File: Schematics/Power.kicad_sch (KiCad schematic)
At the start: 12 parts, among them J25 43650-0418, J26 43650-0418, J27 43650-0418, U5 TR05S3V3

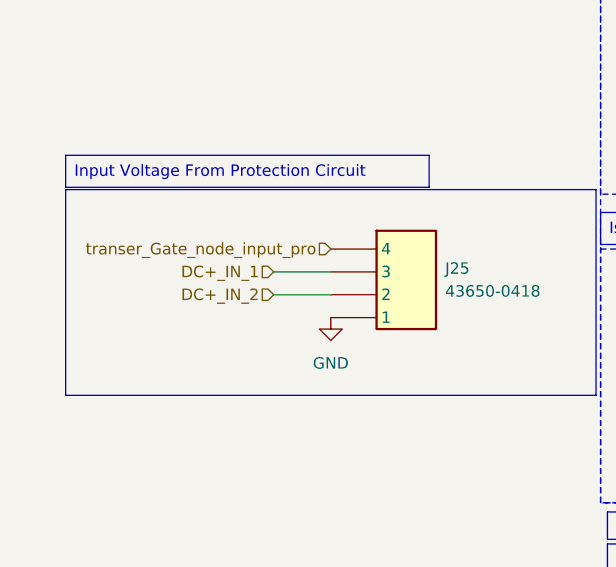
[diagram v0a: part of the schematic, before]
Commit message: WIP PCB Design: Finished DC Input / Protection Circuit
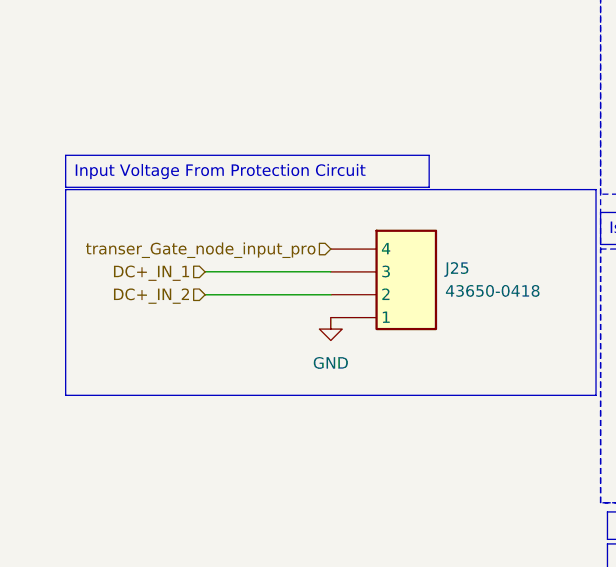
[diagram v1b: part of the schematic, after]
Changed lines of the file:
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@@
 	(wire
 		(pts
-			(xy 46.99 88.9) (xy 53.34 88.9)
+			(xy 39.37 88.9) (xy 53.34 88.9)
 		)
 		(stroke
@@
 	(wire
 		(pts
-			(xy 46.99 86.36) (xy 53.34 86.36)
+			(xy 39.37 86.36) (xy 53.34 86.36)
 		)
 		(stroke
@@
 	(hierarchical_label "DC+_IN_1"
 		(shape input)
-		(at 46.99 86.36 180)
+		(at 39.37 86.36 180)
 		(effects
 			(font
@@
 	(hierarchical_label "DC+_IN_2"
 		(shape input)
-		(at 46.99 88.9 180)
-		(effects
-			(font
-				(size 1.27 1.27)
-			)
-			(justify right)
-		)
-	)
+		(at 39.37 88.9 180)
+		(effects
+			(font
+				(size 1.27 1.27)
+			)
+			(justify right)
+		)
+	)
+	(netclass_flag ""
+		(length 2.54)
+		(shape diamond)
+		(at 97.79 99.06 180)
+		(fields_autoplaced yes)
+		(effects
+			(font
+				(size 1.27 1.27)
+			)
+			(justify right bottom)
+		)
+		(property "Netclass" "5amp"
+			(at 98.9965 101.6 0)
+			(effects
+				(font
+					(size 1.27 1.27)
+				)
+				(justify left)
+			)
+		)
+		(property "Component Class" ""
+			(at -110.49 40.64 0)
+			(effects
+				(font
+					(size 1.27 1.27)
+					(italic yes)
+				)
+			)
+		)
+	)
+	(netclass_flag ""
+		(length 2.54)
+		(shape diamond)
+		(at 41.91 88.9 180)
+		(fields_autoplaced yes)
+		(effects
+			(font
+				(size 1.27 1.27)
+			)
+			(justify right bottom)
+		)
+		(property "Netclass" "5amp"
+			(at 43.1165 91.44 0)
+			(effects
+				(font
+					(size 1.27 1.27)
+				)
+				(justify left)
+			)
+		)
+		(property "Component Class" ""
+			(at -166.37 30.48 0)
+			(effects
+				(font
+					(size 1.27 1.27)
+					(italic yes)
+				)
+			)
+		)
+	)
+	(netclass_flag ""
+		(length 2.54)
+		(shape diamond)
+		(at 45.72 86.36 180)
+		(fields_autoplaced yes)
+		(effects
+			(font
+				(size 1.27 1.27)
+			)
+			(justify right bottom)
+		)
+		(property "Netclass" "5amp"
+			(at 46.9265 88.9 0)
+			(effects
+				(font
+					(size 1.27 1.27)
+				)
+				(justify left)
+			)
+		)
+		(property "Component Class" ""
+			(at -162.56 27.94 0)
+			(effects
+				(font
+					(size 1.27 1.27)
+					(italic yes)
+				)
+			)
+		)
+	)
+	(netclass_flag ""
+		(length 2.54)
+		(shape diamond)
+		(at 97.79 58.42 180)
+		(fields_autoplaced yes)
+		(effects
+			(font
+				(size 1.27 1.27)
+			)
+			(justify right bottom)
+		)
+		(property "Netclass" "5amp"
+			(at 98.9965 60.96 0)
+			(effects
+				(font
+					(size 1.27 1.27)
+				)
+				(justify left)
+			)
+		)
+		(property "Component Class" ""
+			(at -110.49 0 0)
+			(effects
+				(font
+					(size 1.27 1.27)
+					(italic yes)
+				)
+			)
+		)
+	)
+	(netclass_flag ""
+		(length 2.54)
+		(shape diamond)
+		(at 97.79 63.5 180)
+		(fields_autoplaced yes)
+		(effects
+			(font
+				(size 1.27 1.27)
+			)
+			(justify right bottom)
+		)
+		(property "Netclass" "5amp"
+			(at 98.9965 66.04 0)
+			(effects
+				(font
+					(size 1.27 1.27)
+				)
+				(justify left)
+			)
+		)
+		(property "Component Class" ""
+			(at -110.49 5.08 0)
+			(effects
+				(font
+					(size 1.27 1.27)
+					(italic yes)
+				)
+			)
+		)
+	)
+	(netclass_flag ""
+		(length 2.54)
+		(shape diamond)
+		(at 99.06 93.98 180)
+		(fields_autoplaced yes)
+		(effects
+			(font
+				(size 1.27 1.27)
+			)
+			(justify right bottom)
+		)
+		(property "Netclass" "5amp"
+			(at 100.2665 96.52 0)
+			(effects
+				(font
+					(size 1.27 1.27)
+				)
+				(justify left)
+			)
+		)
+		(property "Component Class" ""
+			(at -109.22 35.56 0)
+			(effects
+				(font
+					(size 1.27 1.27)
+					(italic yes)
+				)
+			)
+		)
+	)

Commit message: WIP PCB Design
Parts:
- added H10, H11, H12, H9: MountingHole, MountingHole:MountingHole_2.2mm_M2, symbol Mechanical:MountingHole
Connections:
- net +15V_ISO_LALS: no longer J27.2, PS2.16 (+VO), TP74.1
- new net +15V_ISO_LBLS: J27.2, PS2.16 (+VO), TP74.1

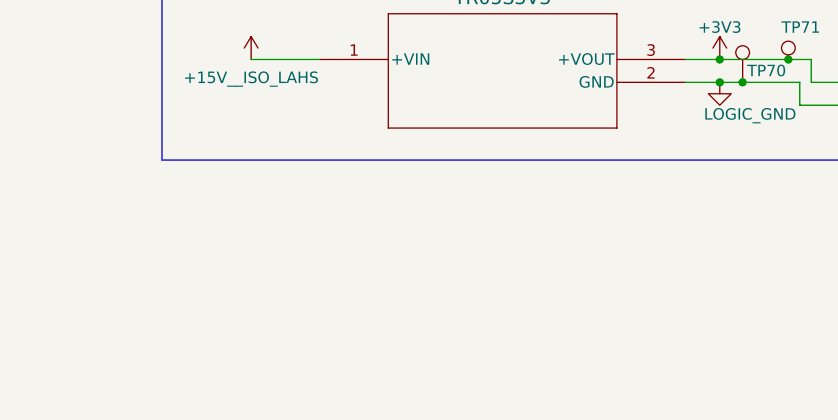
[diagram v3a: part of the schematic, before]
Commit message: Adding two pin connector for 3V3 from power to Full-Bridge
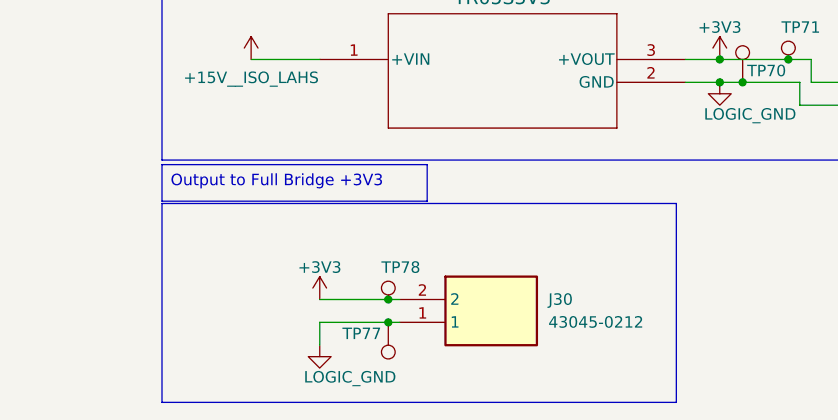
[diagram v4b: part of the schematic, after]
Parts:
- added J30: 43045-0212, 43045-02YY_121314, symbol SiC_Inverter:43045-0212
- added TP77: 5281, SiC_Inverter:5281, symbol SiC_Inverter:5281
- added TP78: 5277, SiC_Inverter:5277, symbol SiC_Inverter:5277
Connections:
- net +3V3: now also J30.2, TP78.1
- net LOGIC_GND: now also J30.1, TP77.1

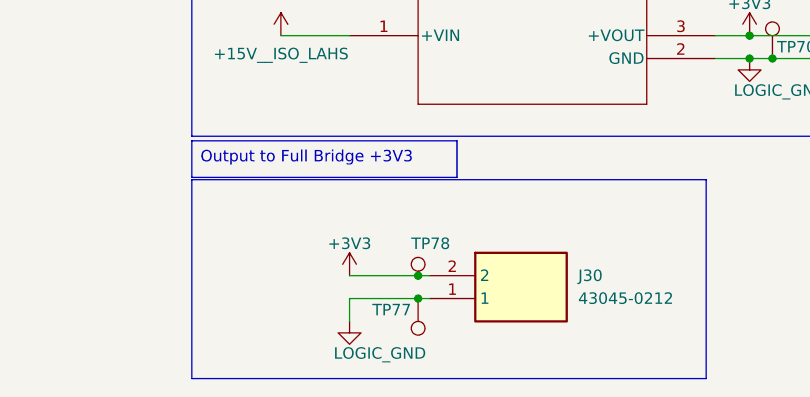
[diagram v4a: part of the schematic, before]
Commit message: Added J30 to the Power Board and new Fab output
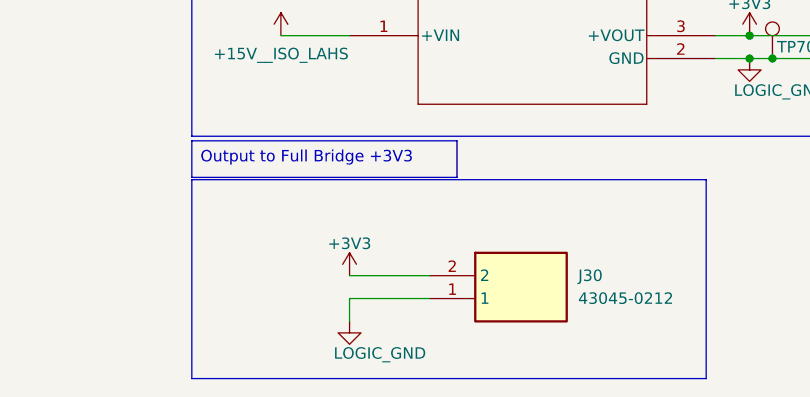
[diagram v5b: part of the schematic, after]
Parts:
- removed TP77: 5281, SiC_Inverter:5281, symbol SiC_Inverter:5281
- removed TP78: 5277, SiC_Inverter:5277, symbol SiC_Inverter:5277
- J30: footprint 43045-02YY_121314 -> SiC_Inverter:43045-0212
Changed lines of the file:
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@@
 	)
 	(junction
-		(at 109.22 157.48)
-		(diameter 0)
-		(color 0 0 0 0)
-	)
-	(junction
 		(at 148.59 130.81)
 		(diameter 0)
@@
 	)
 	(junction
-		(at 109.22 154.94)
-		(diameter 0)
-		(color 0 0 0 0)
-	)
-	(junction
 		(at 165.1 68.58)
 		(diameter 0)
@@
 	(wire
 		(pts
-			(xy 109.22 154.94) (xy 110.49 154.94)
+			(xy 101.6 154.94) (xy 110.49 154.94)
 		)
 		(stroke
@@
 	(wire
 		(pts
-			(xy 101.6 157.48) (xy 109.22 157.48)
+			(xy 101.6 157.48) (xy 110.49 157.48)
 		)
 		(stroke
@@
 	(wire
 		(pts
-			(xy 109.22 157.48) (xy 110.49 157.48)
-		)
-		(stroke
-			(width 0)
-			(type default)
-		)
-	)
-	(wire
-		(pts
 			(xy 142.24 130.81) (xy 146.05 130.81)
 		)
@@
 	(wire
 		(pts
-			(xy 101.6 154.94) (xy 109.22 154.94)
-		)
-		(stroke
-			(width 0)
-			(type default)
-		)
-	)
-	(wire
-		(pts
 			(xy 146.05 130.81) (xy 148.59 130.81)
 		)
@@
 	)
 	(symbol
-		(lib_id "SiC_Inverter:5281")
-		(at 109.22 157.48 180)
-		(unit 1)
-		(body_style 1)
-		(exclude_from_sim no)
-		(in_bom yes)
-		(on_board yes)
-		(in_pos_files yes)
-		(dnp no)
-		(property "Reference" "TP77"
-			(at 108.458 158.75 0)
-			(show_name no)
-			(do_not_autoplace no)
-			(effects
-				(font
-					(size 1.27 1.27)
-				)
-				(justify left)
-			)
-		)
-		(property "Value" "5281"
-			(at 125.222 144.526 0)
-			(hide yes)
-			(show_name no)
-			(do_not_autoplace no)
-			(effects
-				(font
-					(size 1.27 1.27)
-				)
-			)
-		)
-		(property "Footprint" "SiC_Inverter:5281"
-			(at 119.126 146.304 0)
-			(hide yes)
-			(show_name no)
-			(do_not_autoplace no)
-			(effects
-				(font
-					(size 1.27 1.27)
-				)
-			)
-		)
-		(property "Datasheet" "https://www.keyelco.com/userAssets/file/K75p62.pdf"
-			(at 101.346 150.114 0)
-			(hide yes)
-			(show_name no)
-			(do_not_autoplace no)
-			(effects
-				(font
-					(size 1.27 1.27)
-				)
-			)
-		)
-		(property "Description" "Test Plugs & Test Jacks TEST POINT BLACK MULTIPURPOSE"
-			(at 98.806 148.082 0)
-			(hide yes)
-			(show_name no)
-			(do_not_autoplace no)
-			(effects
-				(font
-					(size 1.27 1.27)
-				)
-			)
-		)
-		(pin "1"
-		)
-		(instances
-			(project "SiC_Single_Phase_Inverter"
-				(path "/a1ed0539-9735-4ad1-a8fd-87e26e7fce16/e9f9d5ca-7f9f-4dc3-b303-71fca817b963"
-					(reference "TP77")
-					(unit 1)
-				)
-			)
-		)
-	)
-	(symbol
 		(lib_id "Mechanical:MountingHole")
 		(at 191.77 107.95 0)
@@
 	)
 	(symbol
-		(lib_id "SiC_Inverter:5277")
-		(at 109.22 156.21 0)
-		(unit 1)
-		(body_style 1)
-		(exclude_from_sim no)
-		(in_bom yes)
-		(on_board yes)
-		(in_pos_files yes)
-		(dnp no)
-		(property "Reference" "TP78"
-			(at 108.458 151.384 0)
-			(show_name no)
-			(do_not_autoplace no)
-			(effects
-				(font
-					(size 1.27 1.27)
-				)
-				(justify left)
-			)
-		)
-		(property "Value" "5277"
-			(at 93.218 169.164 0)
-			(hide yes)
-			(show_name no)
-			(do_not_autoplace no)
-			(effects
-				(font
-					(size 1.27 1.27)
-				)
-			)
-		)
-		(property "Footprint" "SiC_Inverter:5277"
-			(at 99.314 167.386 0)
-			(hide yes)
-			(show_name no)
-			(do_not_autoplace no)
-			(effects
-				(font
-					(size 1.27 1.27)
-				)
-			)
-		)
-		(property "Datasheet" "https://www.keyelco.com/userAssets/file/K75p62.pdf"
-			(at 117.094 163.576 0)
-			(hide yes)
-			(show_name no)
-			(do_not_autoplace no)
-			(effects
-				(font
-					(size 1.27 1.27)
-				)
-			)
-		)
-		(property "Description" "Test Plugs & Test Jacks TEST POINT (BLUE) - COMPACT"
-			(at 119.634 165.608 0)
-			(hide yes)
-			(show_name no)
-			(do_not_autoplace no)
-			(effects
-				(font
-					(size 1.27 1.27)
-				)
-			)
-		)
-		(pin "1"
-		)
-		(instances
-			(project "SiC_Single_Phase_Inverter"
-				(path "/a1ed0539-9735-4ad1-a8fd-87e26e7fce16/e9f9d5ca-7f9f-4dc3-b303-71fca817b963"
-					(reference "TP78")
-					(unit 1)
-				)
-			)
-		)
-	)
-	(symbol
 		(lib_id "power:GND")
 		(at 134.62 105.41 0)
@@
 			)
 		)
-		(property "Footprint" "43045-02YY_121314"
+		(property "Footprint" "SiC_Inverter:43045-0212"
 			(at 127 249.86 0)
 			(hide yes)
